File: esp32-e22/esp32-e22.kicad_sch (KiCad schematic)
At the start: 10 parts, among them J1 Conn_01x04_Socket, J2 Conn_01x04_Socket, J3 Conn_01x04_Socket, J4 Conn_01x03_Socket, SW1 SW_Push, U2 ESP32-DevKitC

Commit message: update
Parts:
- added J5: SMA, Connector_Coaxial:SMA_Amphenol_901-143_Horizontal, symbol Connector:Conn_Coaxial
- added J6: Conn_01x01_Socket, Connector_PinHeader_2.54mm:PinHeader_1x01_P2.54mm_Vertical, symbol Connector:Conn_01x01_Socket
- J1, J2, J3: footprint (none) -> Connector_PinHeader_2.54mm:PinHeader_1x04_P2.54mm_Vertical
- J4: footprint (none) -> Connector_PinHeader_2.54mm:PinHeader_1x03_P2.54mm_Vertical
- U1: value ~ -> E22-40033S; footprint Parts:E22-400M33S -> E22:E22-400M33S
- U2: footprint PCM_Espressif:ESP32-DevKitC -> E22:ESP32-DevKitC
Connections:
- net +5V: now also U1.9 (VCC)
- net at U1.21 (ANT): now also J5.1 (In)
- net at U1.8 (DIO2): now also J6.1 (Pin_1)
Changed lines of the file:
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@@
 	(wire
 		(pts
+			(xy 229.87 58.42) (xy 229.87 55.88)
+		)
+		(stroke
+			(width 0)
+			(type default)
+		)
+	)
+	(wire
+		(pts
 			(xy 140.97 58.42) (xy 143.51 58.42)
 		)
@@
 	(wire
 		(pts
+			(xy 222.25 58.42) (xy 229.87 58.42)
+		)
+		(stroke
+			(width 0)
+			(type default)
+		)
+	)
+	(wire
+		(pts
 			(xy 224.79 71.12) (xy 224.79 81.28)
 		)
@@
 	(wire
 		(pts
+			(xy 193.04 83.82) (xy 199.39 83.82)
+		)
+		(stroke
+			(width 0)
+			(type default)
+		)
+	)
+	(wire
+		(pts
+			(xy 222.25 60.96) (xy 234.95 60.96)
+		)
+		(stroke
+			(width 0)
+			(type default)
+		)
+	)
+	(wire
+		(pts
 			(xy 199.39 53.34) (xy 198.12 53.34)
 		)
@@
 			)
 		)
-		(property "Footprint" ""
+		(property "Footprint" "Connector_PinHeader_2.54mm:PinHeader_1x04_P2.54mm_Vertical"
 			(at 60.96 162.56 0)
 			(effects
@@
 			)
 		)
-		(property "Footprint" "PCM_Espressif:ESP32-DevKitC"
+		(property "Footprint" "E22:ESP32-DevKitC"
 			(at 107.95 109.22 0)
 			(effects
@@
 			)
 		)
-		(property "Footprint" ""
+		(property "Footprint" "Connector_PinHeader_2.54mm:PinHeader_1x03_P2.54mm_Vertical"
 			(at 60.96 180.34 0)
 			(effects
@@
 			)
 		)
-		(property "Footprint" ""
+		(property "Footprint" "Connector_PinHeader_2.54mm:PinHeader_1x04_P2.54mm_Vertical"
 			(at 60.96 144.78 0)
 			(effects
@@
 			)
 		)
-		(property "Footprint" ""
+		(property "Footprint" "Connector_PinHeader_2.54mm:PinHeader_1x04_P2.54mm_Vertical"
 			(at 60.96 128.27 0)
 			(effects
@@
 	)
 	(symbol
+		(lib_id "Connector:Conn_01x01_Socket")
+		(at 240.03 60.96 0)
+		(unit 1)
+		(exclude_from_sim no)
+		(in_bom yes)
+		(on_board yes)
+		(dnp no)
+		(fields_autoplaced yes)
+		(property "Reference" "J6"
+			(at 241.3 59.6899 0)
+			(effects
+				(font
+					(size 1.27 1.27)
+				)
+				(justify left)
+			)
+		)
+		(property "Value" "Conn_01x01_Socket"
+			(at 241.3 62.2299 0)
+			(effects
+				(font
+					(size 1.27 1.27)
+				)
+				(justify left)
+			)
+		)
+		(property "Footprint" "Connector_PinHeader_2.54mm:PinHeader_1x01_P2.54mm_Vertical"
+			(at 240.03 60.96 0)
+			(effects
+				(font
+					(size 1.27 1.27)
+				)
+				(hide yes)
+			)
+		)
+		(property "Datasheet" "~"
+			(at 240.03 60.96 0)
+			(effects
+				(font
+					(size 1.27 1.27)
+				)
+				(hide yes)
+			)
+		)
+		(property "Description" "Generic connector, single row, 01x01, script generated"
+			(at 240.03 60.96 0)
+			(effects
+				(font
+					(size 1.27 1.27)
+				)
+				(hide yes)
+			)
+		)
+		(pin "1"
+		)
+		(instances
+			(project ""
+				(path "/7ac59502-473d-4014-a9ef-f4cf3cefb926"
+					(reference "J6")
+					(unit 1)
+				)
+			)
+		)
+	)
+	(symbol
 		(lib_id "Switch:SW_Push")
 		(at 46.99 48.26 0)
@@
 		(on_board yes)
 		(dnp no)
-		(fields_autoplaced yes)
 		(property "Reference" "U1"
 			(at 210.82 45.085 0)
@@
 					(size 1.27 1.27)
 				)
-				(hide yes)
 			)
 		)
-		(property "Value" "~"
-			(at 210.82 45.72 0)
+		(property "Value" "E22-40033S"
+			(at 210.566 48.006 0)
 			(effects
 				(font
@@
 			)
 		)
-		(property "Footprint" "Parts:E22-400M33S"
+		(property "Footprint" "E22:E22-400M33S"
 			(at 210.82 46.99 0)
 			(effects
@@
 					(size 1.27 1.27)
 				)
+				(hide yes)
 			)
 		)
@@
 					(unit 1)
 				)
+			)
+		)
+	)
+	(symbol
+		(lib_id "Connector:Conn_Coaxial")
+		(at 187.96 83.82 180)
+		(unit 1)
+		(exclude_from_sim no)
+		(in_bom yes)
+		(on_board yes)
+		(dnp no)
+		(fields_autoplaced yes)
+		(property "Reference" "J5"
+			(at 184.15 82.2567 0)
+			(effects
+				(font
+					(size 1.27 1.27)
+				)
+				(justify left)
+			)
+		)
+		(property "Value" "SMA"
+			(at 184.15 84.7967 0)
+			(effects
+				(font
+					(size 1.27 1.27)
+				)
+				(justify left)
+			)
+		)
+		(property "Footprint" "Connector_Coaxial:SMA_Amphenol_901-143_Horizontal"
+			(at 187.96 83.82 0)
+			(effects
+				(font
+					(size 1.27 1.27)
+				)
+				(hide yes)
+			)
+		)
+		(property "Datasheet" "~"
+			(at 187.96 83.82 0)
+			(effects
+				(font
+					(size 1.27 1.27)
+				)
+				(hide yes)
+			)
+		)
+		(property "Description" "coaxial connector (BNC, SMA, SMB, SMC, Cinch/RCA, LEMO, ...)"
+			(at 187.96 83.82 0)
+			(effects
+				(font
+					(size 1.27 1.27)
+				)
+				(hide yes)
+			)
+		)
+		(pin "1"
+		)
+		(pin "2"
+		)
+		(instances
+			(project ""
+				(path "/7ac59502-473d-4014-a9ef-f4cf3cefb926"
+					(reference "J5")
+					(unit 1)
+				)

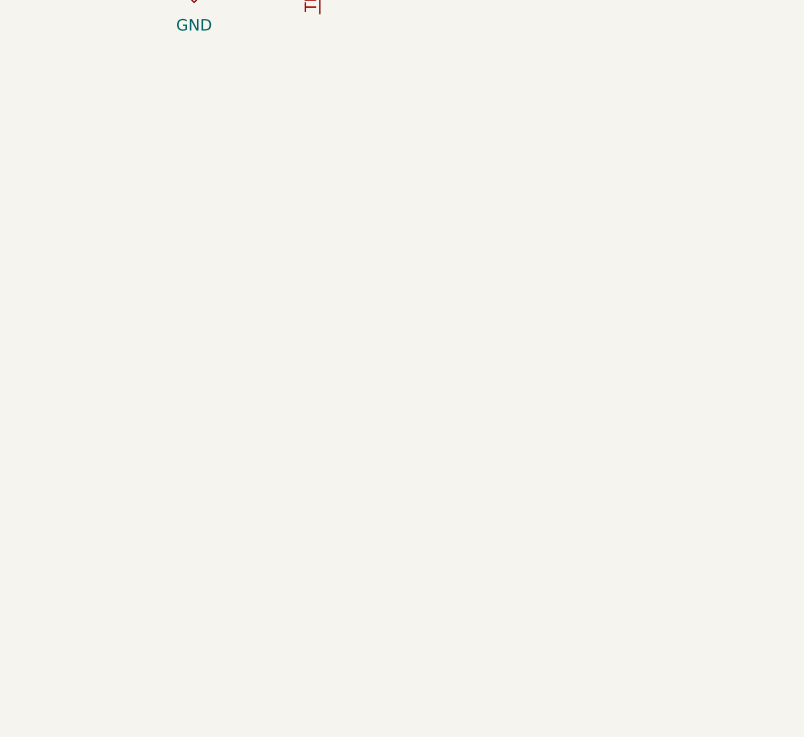
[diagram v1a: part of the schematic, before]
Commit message: add usb-c connector
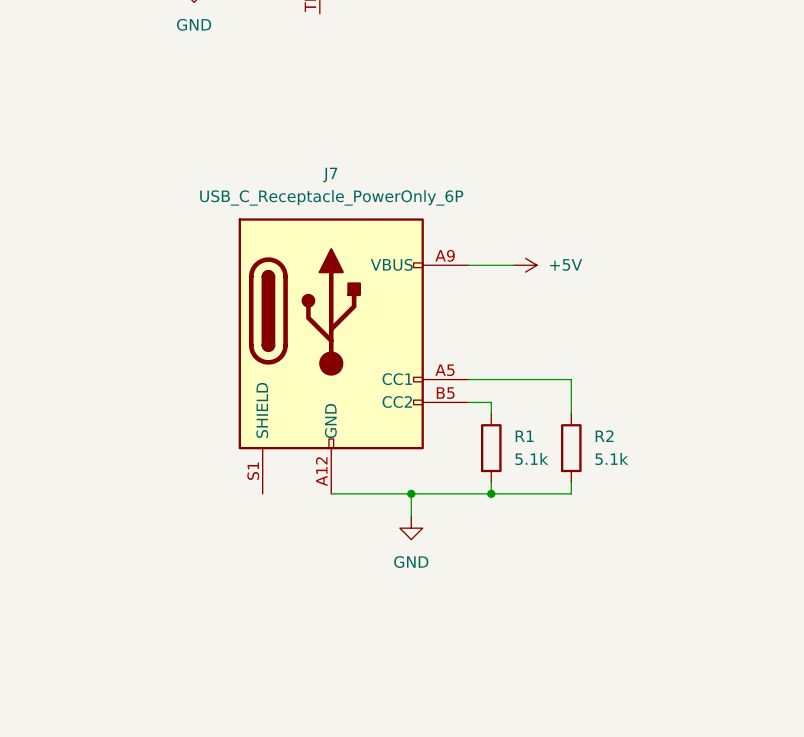
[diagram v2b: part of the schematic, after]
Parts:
- added J7: USB_C_Receptacle_PowerOnly_6P, Connector_USB:USB_C_Receptacle_GCT_USB4125-xx-x-0190_6P_TopMnt_Horizontal, symbol Connector:USB_C_Receptacle_PowerOnly_6P
- added R1, R2: 5.1k, symbol Device:R
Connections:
- net +5V: now also J7.A9 (VBUS), J7.B9 (VBUS)
- net GND: now also J7.A12 (GND), J7.B12 (GND), R1.2, R2.2
- new net: J7.A5 (CC1), R2.1
- new net: J7.B5 (CC2), R1.1

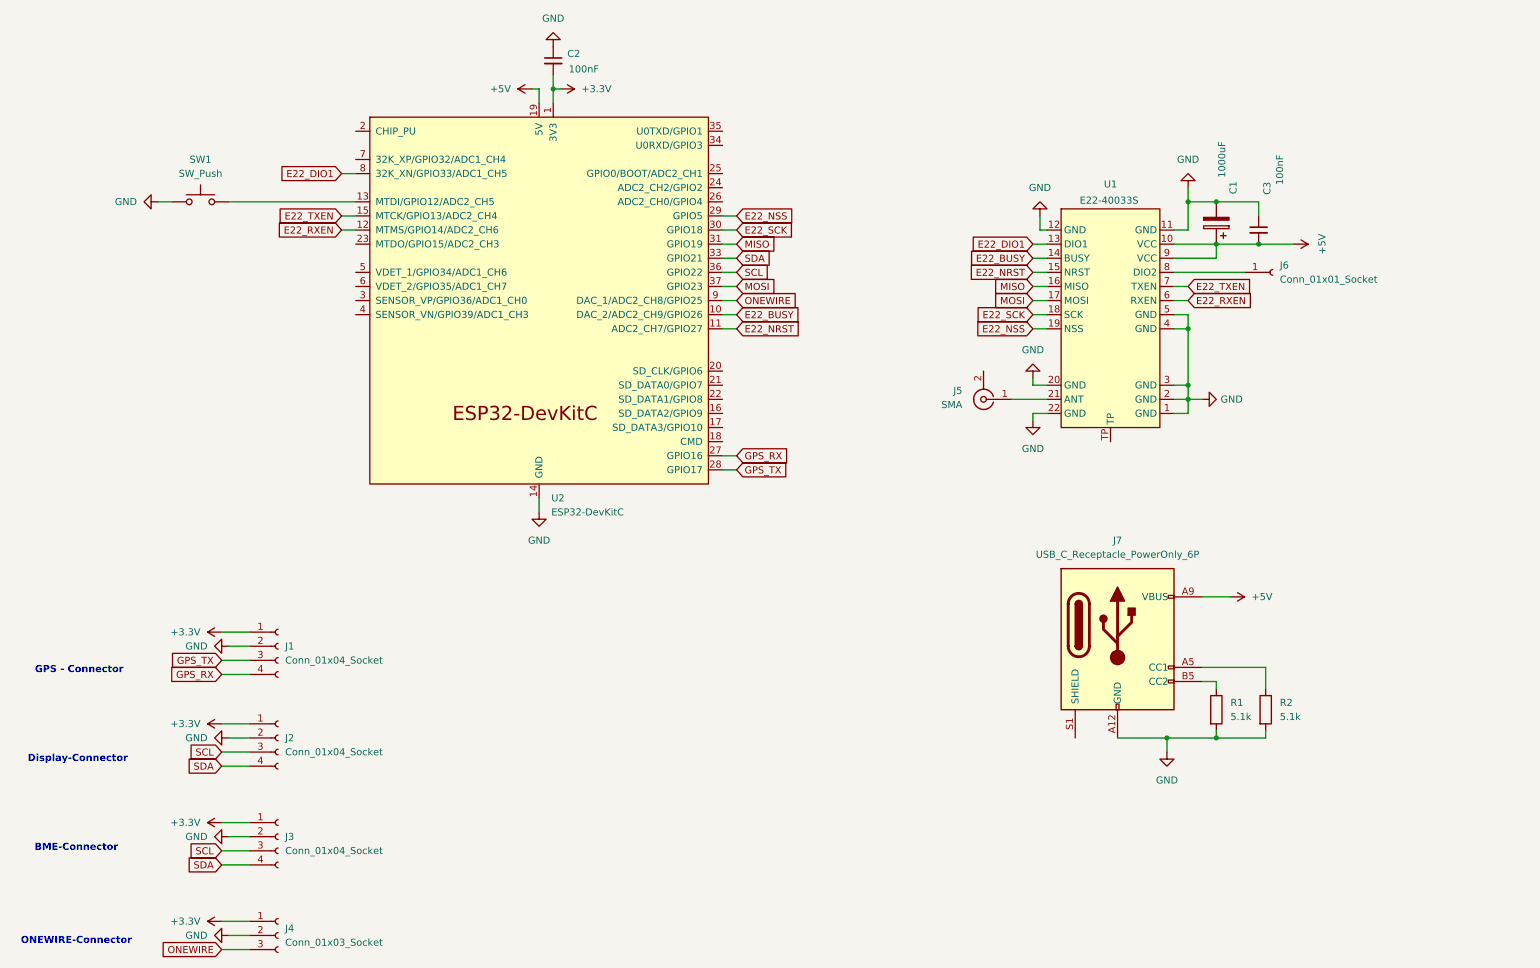
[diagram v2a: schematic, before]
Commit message: update to OE3WAS V2.0.2
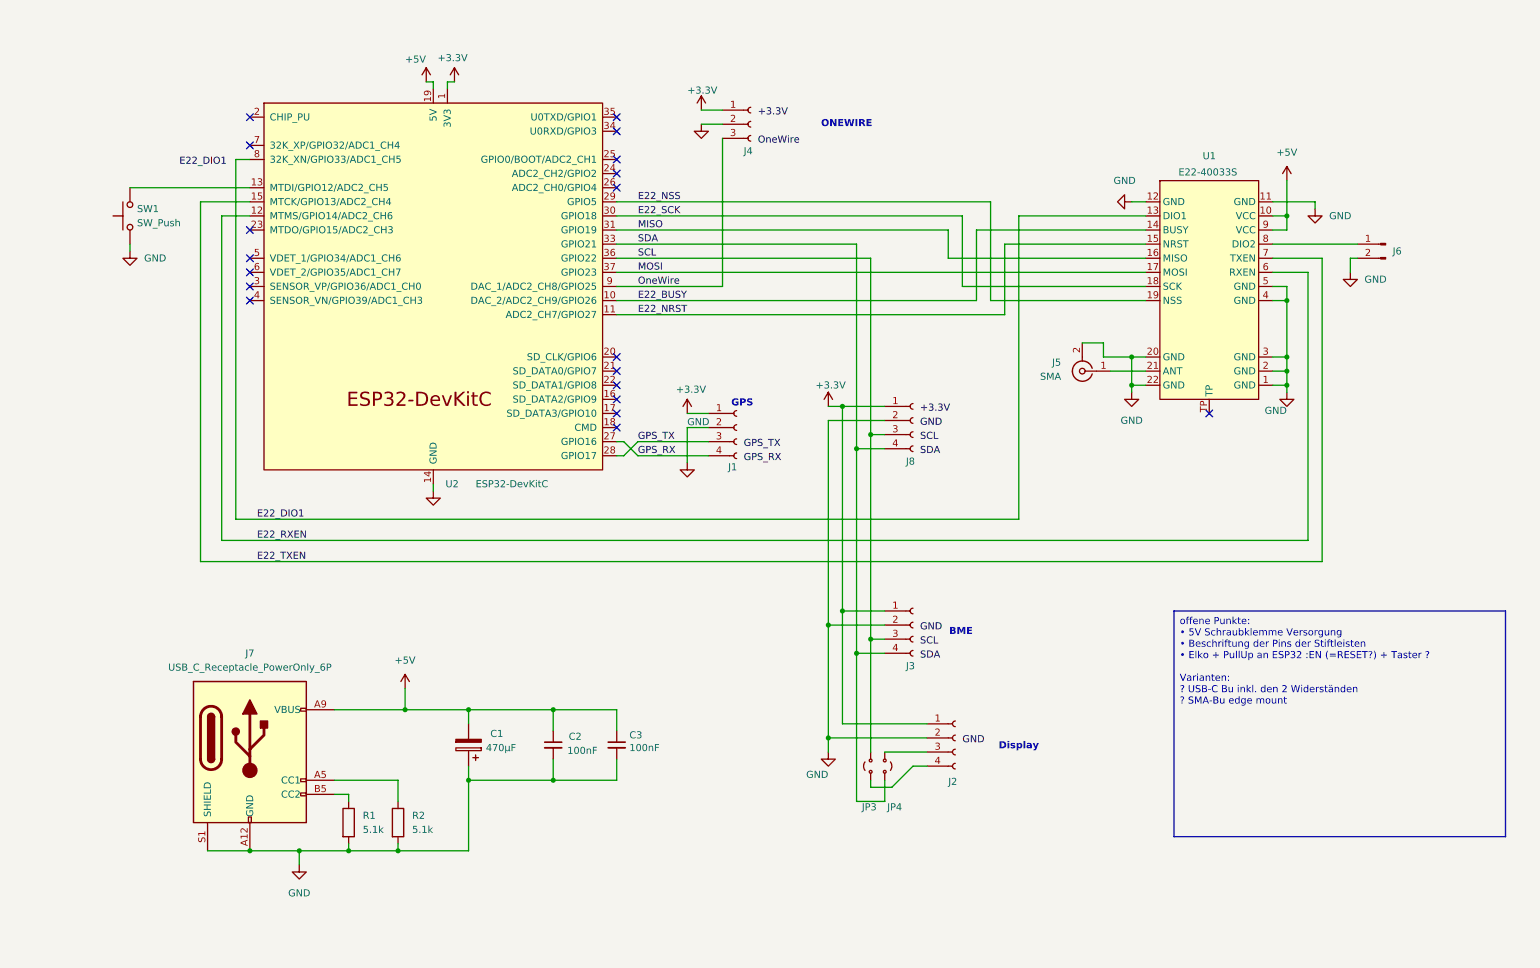
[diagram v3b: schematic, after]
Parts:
- removed J6: Conn_01x01_Socket, Connector_PinHeader_2.54mm:PinHeader_1x01_P2.54mm_Vertical, symbol Connector:Conn_01x01_Socket
- added J6: Conn_01x02_Pin, Connector_PinHeader_2.54mm:PinHeader_1x02_P2.54mm_Vertical, symbol Connector:Conn_01x02_Pin
- added J8: Conn_01x04_Socket, Connector_PinHeader_2.54mm:PinHeader_1x04_P2.54mm_Vertical, symbol Connector:Conn_01x04_Socket
- added JP3, JP4: Jumper_2_Small_Open, TestPoint:TestPoint_2Pads_Pitch2.54mm_Drill0.8mm, symbol Jumper:Jumper_2_Small_Open
- C1: value 1000uF -> 470µF; footprint (none) -> Capacitor_THT:CP_Radial_D8.0mm_P5.00mm
- C2, C3: footprint (none) -> Capacitor_THT:C_Disc_D4.7mm_W2.5mm_P5.00mm
- R1, R2: footprint (none) -> Resistor_THT:R_Axial_DIN0207_L6.3mm_D2.5mm_P7.62mm_Horizontal
- SW1: footprint (none) -> Button_Switch_THT:SW_PUSH_6mm
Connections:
- net +3.3V: now also J8.1 (Pin_1); no longer C2.2
- net +5V: now also C1.2, C2.1, C3.1; no longer C1.1, C3.2
- net GND: now also C1.1, C2.2, C3.2, J5.2 (Ext), J7.S1 (SHIELD), J6.2 (Pin_2), J8.2 (Pin_2); no longer C1.2, C2.1, C3.1
- net SCL: now also J8.3 (Pin_3), JP3.2 (B); no longer J2.3 (Pin_3)
- net SDA: now also J8.4 (Pin_4), JP4.2 (B); no longer J2.4 (Pin_4)
- net at U1.8 (DIO2): now also J6.1 (Pin_1)
- net ONEWIRE renamed OneWire
- new net: J2.3 (Pin_3), JP4.1 (A)
- new net: J2.4 (Pin_4), JP3.1 (A)
- no-connect marks 0 -> 19
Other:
- note added: "BME"
- note added: "Display"
- note added: "GPS"
- note added: "ONEWIRE"
- note removed: "BME-Connector"
- note removed: "Display-Connector"
- note removed: "GPS - Connector"
- note removed: "ONEWIRE-Connector"
- moved on the sheet: J1, J2, J3, J4, J5, J7, R1, R2, SW1, U1, U2

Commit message: update to OE3WAS V2.0.3
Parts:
- removed JP3, JP4: Jumper_2_Small_Open, TestPoint:TestPoint_2Pads_Pitch2.54mm_Drill0.8mm, symbol Jumper:Jumper_2_Small_Open
- added C4: 100nF, Capacitor_THT:C_Disc_D4.7mm_W2.5mm_P5.00mm, symbol Device:C_Small
- added J9: Conn_01x02_Pin, symbol Connector:Conn_01x02_Pin
- added JP1, JP2: Jumper_2_Small_Bridged, TestPoint:TestPoint_2Pads_Pitch2.54mm_Drill0.8mm, symbol Jumper:Jumper_2_Small_Bridged
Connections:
- net +3.3V: now also JP2.1 (A); no longer J2.1 (Pin_1)
- net +5V: now also C4.1, J9.1 (Pin_1)
- net GND: now also C4.2, J9.2 (Pin_2), JP1.1 (A); no longer J2.2 (Pin_2)
- net SCL: now also J2.3 (Pin_3)
- net SDA: now also J2.4 (Pin_4)
- new net: J2.1 (Pin_1), JP2.2 (B)
- new net: J2.2 (Pin_2), JP1.2 (B)
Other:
- note added: "ext. Power 5V DC"
- moved on the sheet: C1, C2, C3, J2, J7, R1, R2

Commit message: update to V2.0.4 (fixed ERC Fails in schematic)
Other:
- note added: "+3.3V"
- note added: "E22_DIO1"
- note added: "GND"
- note added: "GPS_RX"
- note added: "GPS_TX"
- note added: "OneWire"
- note added: "SCL"
- note added: "SDA"
- company: DK9BT -> DK9BT / OE3WAS
